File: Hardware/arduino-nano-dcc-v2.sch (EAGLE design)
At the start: 40 parts, among them IC1 7805TV, IC2 7805TV, IC3 MEGA328-P, X1 22-23-2031

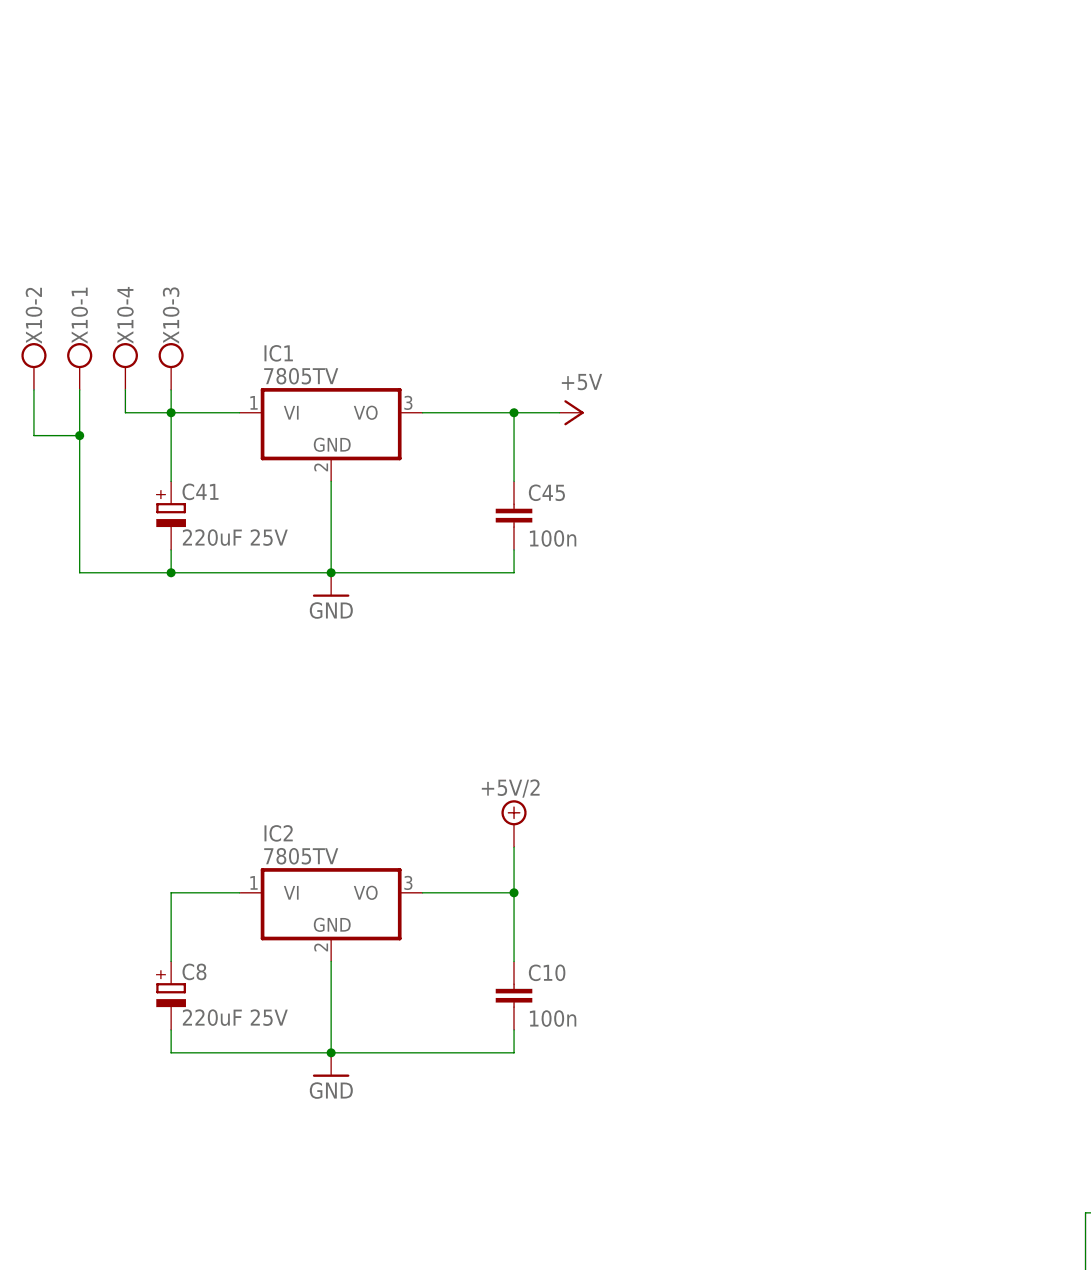
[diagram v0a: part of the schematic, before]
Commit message: Changes  * Added TIP for 5V supply servo's,  * Initial routing.
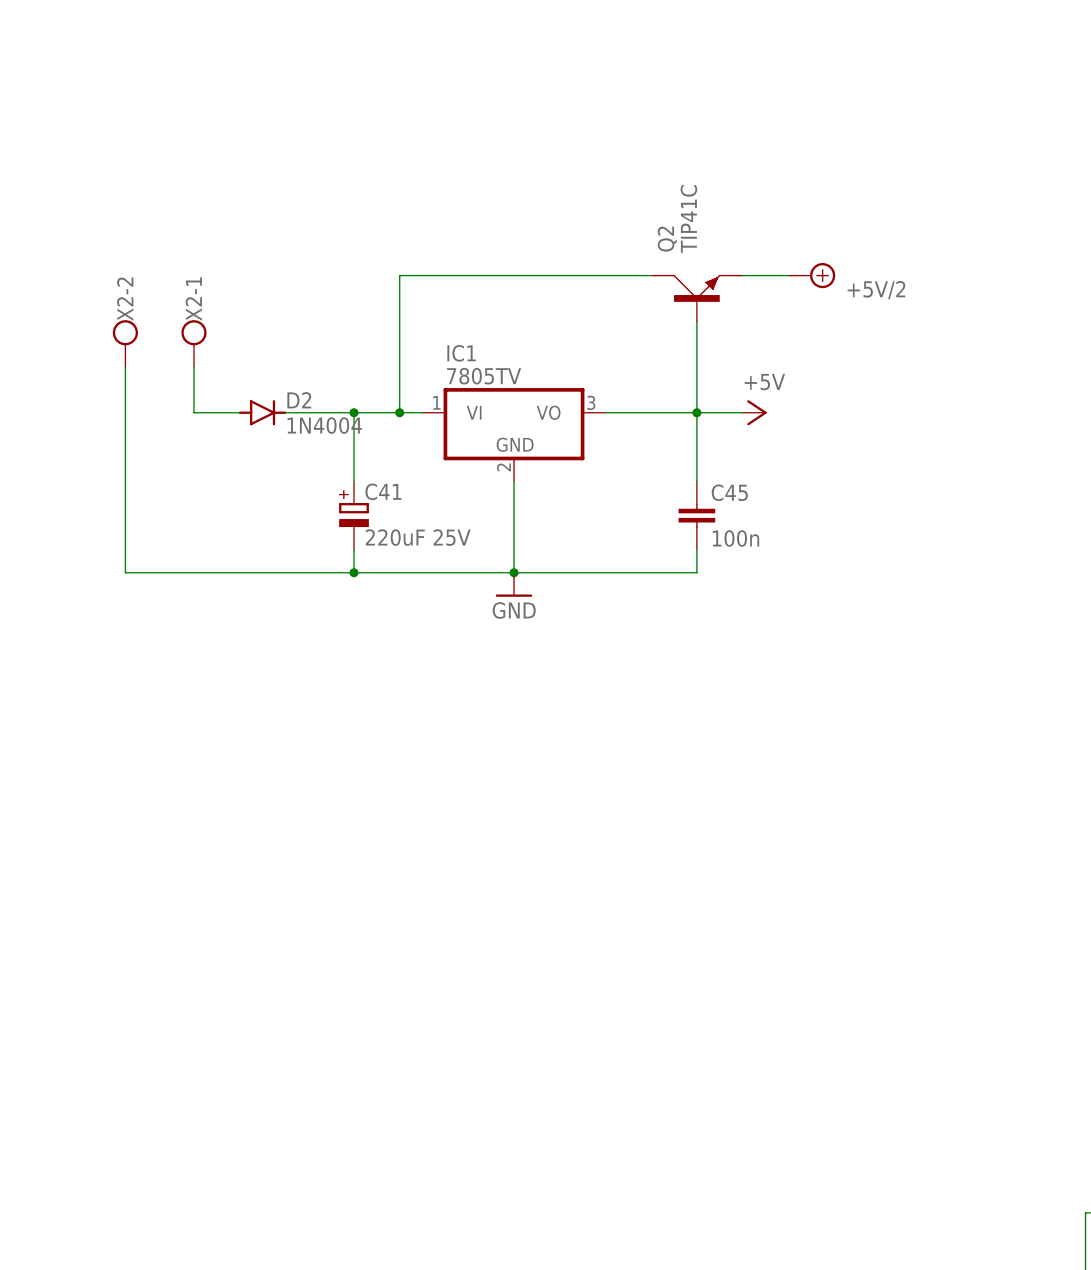
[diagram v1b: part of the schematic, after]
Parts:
- removed C10: 100n, rcl:C-EU050-024X044
- removed C8: 220uF 25V, rcl:CPOL-EUE5-8.5
- removed IC2: 7805TV, linear:7805TV
- removed X10: (no value), con-wago-500:W237-4
- added D2: 1N4004, diode:1N4004
- added Q2: TIP41C, transistor-power:TIP41C
- added X2: (no value), con-wago-500:W237-102
- C4, C6, C7: device rcl:C-EU050-025X075 -> rcl:C-EU050-024X044
- D1: device diode:1N4148DO35-10 -> diode:1N4148DO35-7
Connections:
- net +5V: now also Q2.B
- net +5V/2: now also Q2.E; no longer C10.1, IC2.VO
- net GND: now also X2-2.KL; no longer C10.2, C8.-, IC2.GND, X10-1.KL, X10-2.KL
- net N$1: now also D2.C, Q2.C; no longer X10-3.KL, X10-4.KL
- net N$2: now also D2.A, X2-1.KL; no longer C8.+, IC2.VI
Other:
- moved on the sheet: C41, C45, IC1

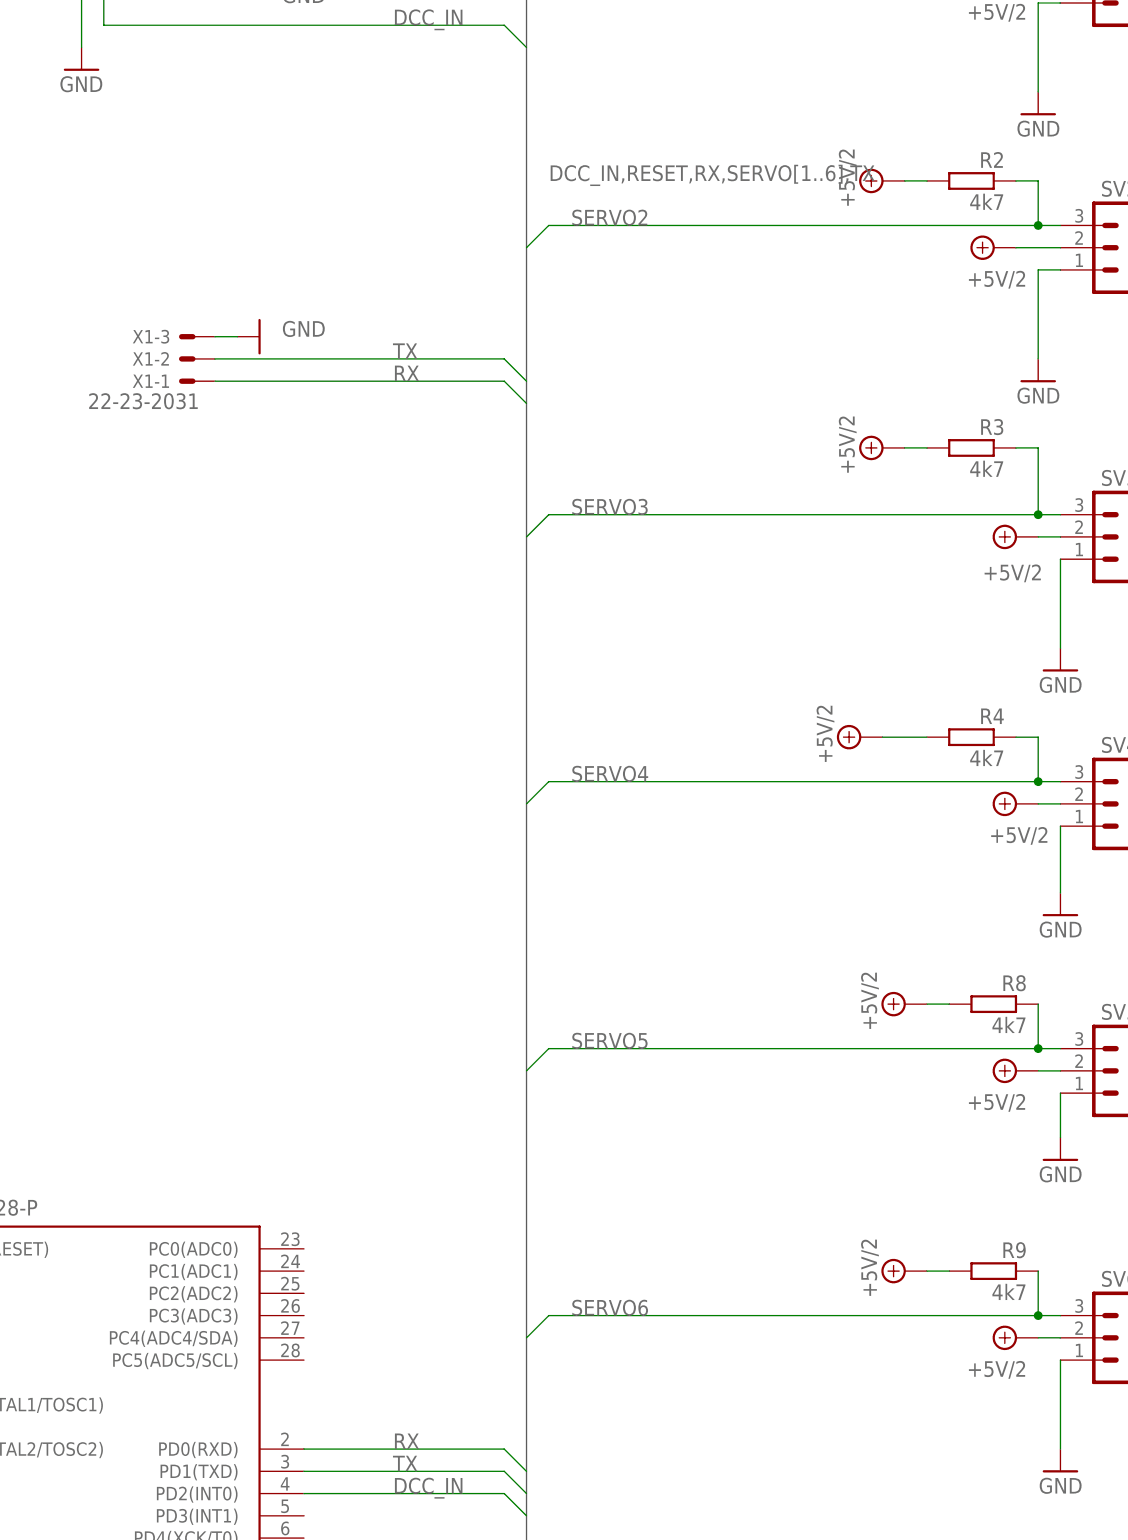
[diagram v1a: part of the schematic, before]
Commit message: Changes :  * Last traces routed.  * Extended to 8 servo's  * PCB somewhat bigger so 8 servo connections fit between the mounting holes.
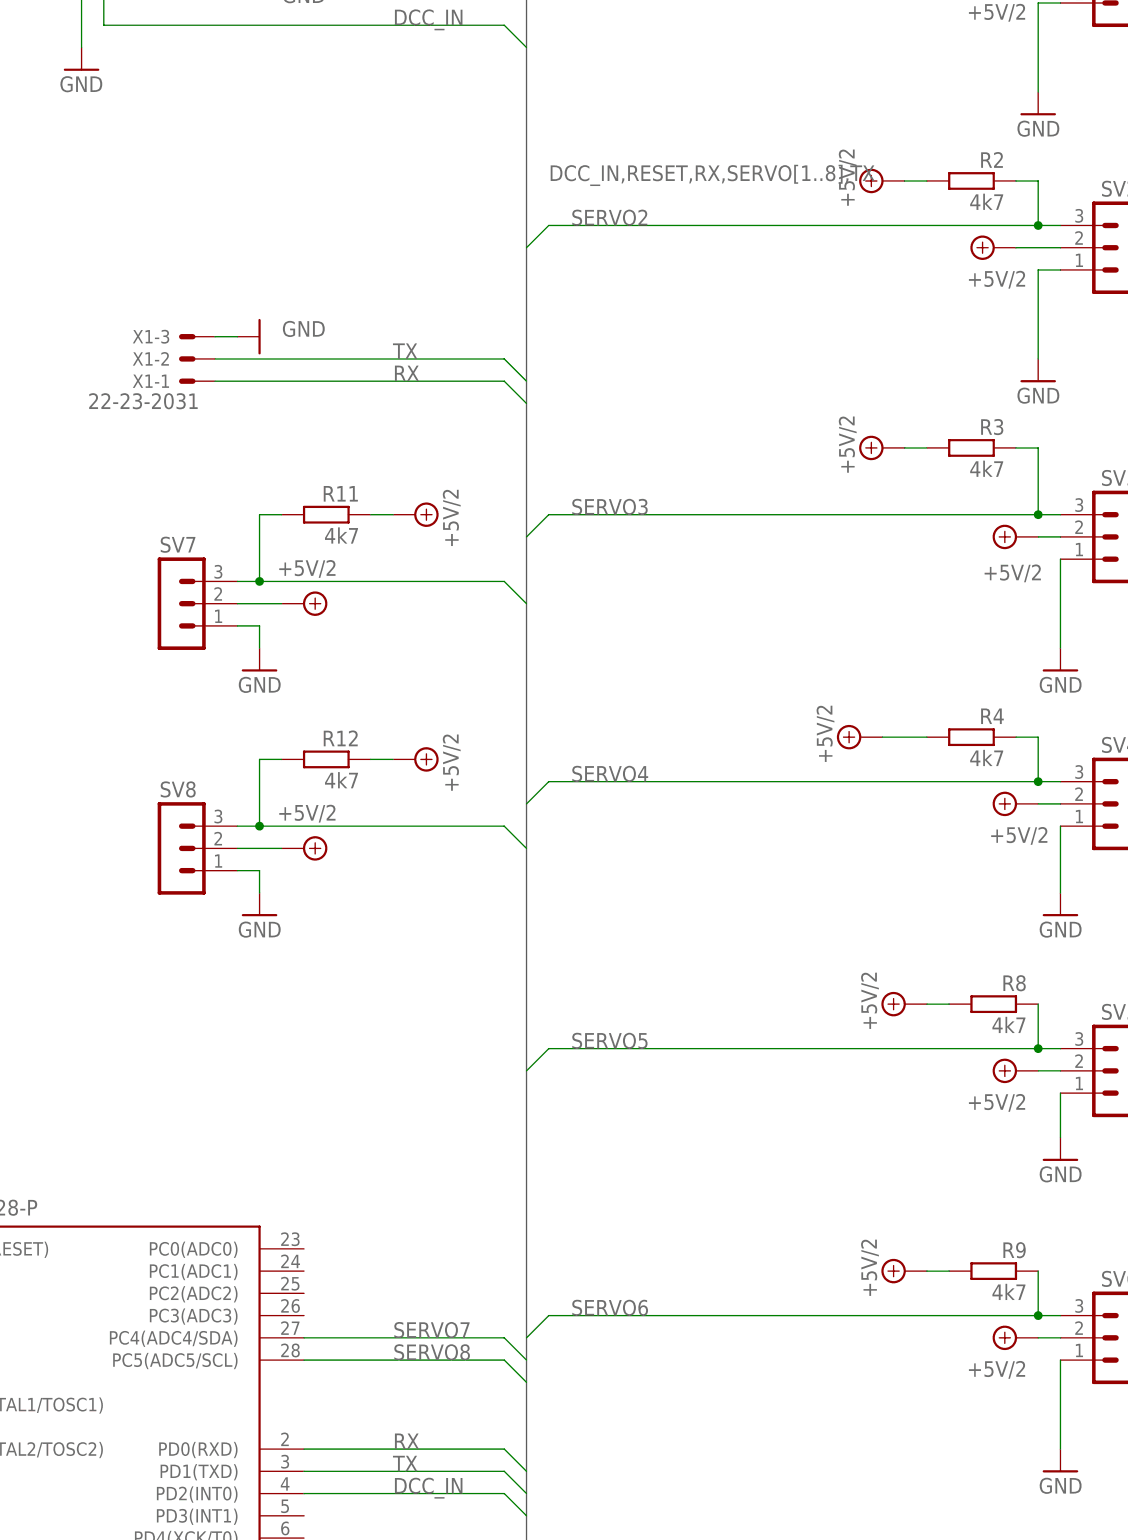
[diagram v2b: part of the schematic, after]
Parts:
- added R11: 4k7, rcl:R-EU_0204/7
- added R12: 4k7, rcl:R-EU_0204/5
- added SV7, SV8: (no value), con-lstb:MA03-1
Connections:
- new net SERVO7: IC3.PC4(ADC4/SDA), R11.2, SV7.3
- new net SERVO8: IC3.PC5(ADC5/SCL), R12.2, SV8.3
- net +5V/2: now also R11.1, R12.1, SV7.2, SV8.2
- net GND: now also SV7.1, SV8.1
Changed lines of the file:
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@@
 <part name="X2" library="con-wago-500" library_urn="urn:adsk.eagle:library:195" deviceset="W237-102" device="" package3d_urn="urn:adsk.eagle:package:10688/1"/>
 <part name="D2" library="diode" library_urn="urn:adsk.eagle:library:210" deviceset="1N4004" device="" package3d_urn="urn:adsk.eagle:package:43336/1"/>
+<part name="SV7" library="con-lstb" deviceset="MA03-1" device=""/>
+<part name="R11" library="rcl" deviceset="R-EU_" device="0204/7" value="4k7"/>
+<part name="SUPPLY8" library="supply2" library_urn="urn:adsk.eagle:library:372" deviceset="+5V/2" device=""/>
+<part name="SUPPLY9" library="supply2" library_urn="urn:adsk.eagle:library:372" deviceset="+5V/2" device=""/>
+<part name="GND17" library="supply1" deviceset="GND" device=""/>
+<part name="SV8" library="con-lstb" deviceset="MA03-1" device=""/>
+<part name="GND19" library="supply1" deviceset="GND" device=""/>
+<part name="SUPPLY16" library="supply2" library_urn="urn:adsk.eagle:library:372" deviceset="+5V/2" device=""/>
+<part name="SUPPLY17" library="supply2" library_urn="urn:adsk.eagle:library:372" deviceset="+5V/2" device=""/>
+<part name="R12" library="rcl" deviceset="R-EU_" device="0204/5" value="4k7"/>
 </parts>
 <sheets>
@@
 <attribute name="VALUE" x="35.56" y="170.4086" size="1.778" layer="96"/>
 </instance>
+<instance part="SV7" gate="G$1" x="218.44" y="157.48" smashed="yes">
+<attribute name="VALUE" x="217.17" y="149.86" size="1.778" layer="96"/>
+<attribute name="NAME" x="217.17" y="163.322" size="1.778" layer="95"/>
+</instance>
+<instance part="R11" gate="G$1" x="236.22" y="167.64" smashed="yes" rot="MR0">
+<attribute name="NAME" x="240.03" y="169.1386" size="1.778" layer="95" rot="MR0"/>
+<attribute name="VALUE" x="240.03" y="164.338" size="1.778" layer="96" rot="MR0"/>
+</instance>
+<instance part="SUPPLY8" gate="G$1" x="246.38" y="167.64" smashed="yes" rot="MR90">
+<attribute name="VALUE" x="249.555" y="163.83" size="1.778" layer="96" rot="MR90"/>
+</instance>
+<instance part="SUPPLY9" gate="G$1" x="233.68" y="157.48" smashed="yes" rot="MR90">
+<attribute name="VALUE" x="237.49" y="160.655" size="1.778" layer="96" rot="MR0"/>
+</instance>
+<instance part="GND17" gate="1" x="228.6" y="149.86" smashed="yes" rot="MR0">
+<attribute name="VALUE" x="231.14" y="147.32" size="1.778" layer="96" rot="MR0"/>
+</instance>
+<instance part="SV8" gate="G$1" x="218.44" y="129.54" smashed="yes">
+<attribute name="VALUE" x="217.17" y="121.92" size="1.778" layer="96"/>
+<attribute name="NAME" x="217.17" y="135.382" size="1.778" layer="95"/>
+</instance>
+<instance part="GND19" gate="1" x="228.6" y="121.92" smashed="yes" rot="MR0">
+<attribute name="VALUE" x="231.14" y="119.38" size="1.778" layer="96" rot="MR0"/>
+</instance>
+<instance part="SUPPLY16" gate="G$1" x="233.68" y="129.54" smashed="yes" rot="MR90">
+<attribute name="VALUE" x="237.49" y="132.715" size="1.778" layer="96" rot="MR0"/>
+</instance>
+<instance part="SUPPLY17" gate="G$1" x="246.38" y="139.7" smashed="yes" rot="MR90">
+<attribute name="VALUE" x="249.555" y="135.89" size="1.778" layer="96" rot="MR90"/>
+</instance>
+<instance part="R12" gate="G$1" x="236.22" y="139.7" smashed="yes" rot="MR0">
+<attribute name="NAME" x="240.03" y="141.1986" size="1.778" layer="95" rot="MR0"/>
+<attribute name="VALUE" x="240.03" y="136.398" size="1.778" layer="96" rot="MR0"/>
+</instance>
 </instances>
 <busses>
-<bus name="DCC_IN,RESET,RX,SERVO[1..6],TX">
+<bus name="DCC_IN,RESET,RX,SERVO[1..8],TX">
 <segment>
 <wire x1="259.08" y1="243.84" x2="259.08" y2="17.78" width="0.762" layer="92"/>
@@
 <wire x1="124.46" y1="38.1" x2="124.46" y2="43.18" width="0.1524" layer="91"/>
 </segment>
+<segment>
+<pinref part="SV8" gate="G$1" pin="1"/>
+<wire x1="226.06" y1="127" x2="228.6" y2="127" width="0.1524" layer="91"/>
+<pinref part="GND19" gate="1" pin="GND"/>
+<wire x1="228.6" y1="127" x2="228.6" y2="124.46" width="0.1524" layer="91"/>
+</segment>
+<segment>
+<pinref part="SV7" gate="G$1" pin="1"/>
+<wire x1="226.06" y1="154.94" x2="228.6" y2="154.94" width="0.1524" layer="91"/>
+<pinref part="GND17" gate="1" pin="GND"/>
+<wire x1="228.6" y1="154.94" x2="228.6" y2="152.4" width="0.1524" layer="91"/>
+</segment>
 </net>
 <net name="N$17" class="0">
@@
 <pinref part="SUPPLY7" gate="G$1" pin="+5V/2"/>
 <wire x1="91.44" y1="187.96" x2="86.36" y2="187.96" width="0.1524" layer="91"/>
+</segment>
+<segment>
+<pinref part="R11" gate="G$1" pin="1"/>
+<pinref part="SUPPLY8" gate="G$1" pin="+5V/2"/>
+<wire x1="243.84" y1="167.64" x2="241.3" y2="167.64" width="0.1524" layer="91"/>
+</segment>
+<segment>
+<pinref part="SV7" gate="G$1" pin="2"/>
+<pinref part="SUPPLY9" gate="G$1" pin="+5V/2"/>
+<wire x1="231.14" y1="157.48" x2="226.06" y2="157.48" width="0.1524" layer="91"/>
+</segment>
+<segment>
+<pinref part="R12" gate="G$1" pin="1"/>
+<pinref part="SUPPLY17" gate="G$1" pin="+5V/2"/>
+<wire x1="243.84" y1="139.7" x2="241.3" y2="139.7" width="0.1524" layer="91"/>
+</segment>
+<segment>
+<pinref part="SV8" gate="G$1" pin="2"/>
+<pinref part="SUPPLY16" gate="G$1" pin="+5V/2"/>
+<wire x1="231.14" y1="129.54" x2="226.06" y2="129.54" width="0.1524" layer="91"/>
 </segment>
 </net>
@@
 </segment>
 </net>
+<net name="SERVO7" class="0">
+<segment>
+<wire x1="259.08" y1="157.48" x2="256.54" y2="160.02" width="0.1524" layer="91"/>
+<pinref part="SV7" gate="G$1" pin="3"/>
+<wire x1="256.54" y1="160.02" x2="228.6" y2="160.02" width="0.1524" layer="91"/>
+<pinref part="R11" gate="G$1" pin="2"/>
+<wire x1="228.6" y1="160.02" x2="226.06" y2="160.02" width="0.1524" layer="91"/>
+<wire x1="231.14" y1="167.64" x2="228.6" y2="167.64" width="0.1524" layer="91"/>
+<wire x1="228.6" y1="167.64" x2="228.6" y2="160.02" width="0.1524" layer="91"/>
+<junction x="228.6" y="160.02"/>
+</segment>
+<segment>
+<wire x1="259.08" y1="71.12" x2="256.54" y2="73.66" width="0.1524" layer="91"/>
+<pinref part="IC3" gate="G$1" pin="PC4(ADC4/SDA)"/>
+<wire x1="256.54" y1="73.66" x2="233.68" y2="73.66" width="0.1524" layer="91"/>
+<label x="243.84" y="73.66" size="1.778" layer="95"/>
+</segment>
+</net>
+<net name="SERVO8" class="0">
+<segment>
+<wire x1="259.08" y1="129.54" x2="256.54" y2="132.08" width="0.1524" layer="91"/>
+<pinref part="SV8" gate="G$1" pin="3"/>
+<wire x1="256.54" y1="132.08" x2="228.6" y2="132.08" width="0.1524" layer="91"/>
+<pinref part="R12" gate="G$1" pin="2"/>
+<wire x1="228.6" y1="132.08" x2="226.06" y2="132.08" width="0.1524" layer="91"/>
+<wire x1="231.14" y1="139.7" x2="228.6" y2="139.7" width="0.1524" layer="91"/>
+<wire x1="228.6" y1="139.7" x2="228.6" y2="132.08" width="0.1524" layer="91"/>
+<junction x="228.6" y="132.08"/>
+</segment>
+<segment>
+<wire x1="259.08" y1="68.58" x2="256.54" y2="71.12" width="0.1524" layer="91"/>
+<pinref part="IC3" gate="G$1" pin="PC5(ADC5/SCL)"/>
+<wire x1="256.54" y1="71.12" x2="233.68" y2="71.12" width="0.1524" layer="91"/>
+<label x="243.84" y="71.12" size="1.778" layer="95"/>
+</segment>
+</net>
